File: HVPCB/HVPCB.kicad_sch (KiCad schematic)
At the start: 53 parts, among them J1 Micro Fit 10p, Q1 OnSemi FDB12N50TM, U1 NE555DR_C695838, U14 Micro Fit 2P, U16 Micro Fit 2P, U2 SN74LVC1GU04DBVR, U3 PDSE1-S5-D5-M-TR, U4 LM392MX, U5 AO3400A, U6 AO3400A, U7 KT-0603R, U8 KT-0603R, U9 KT-0603R

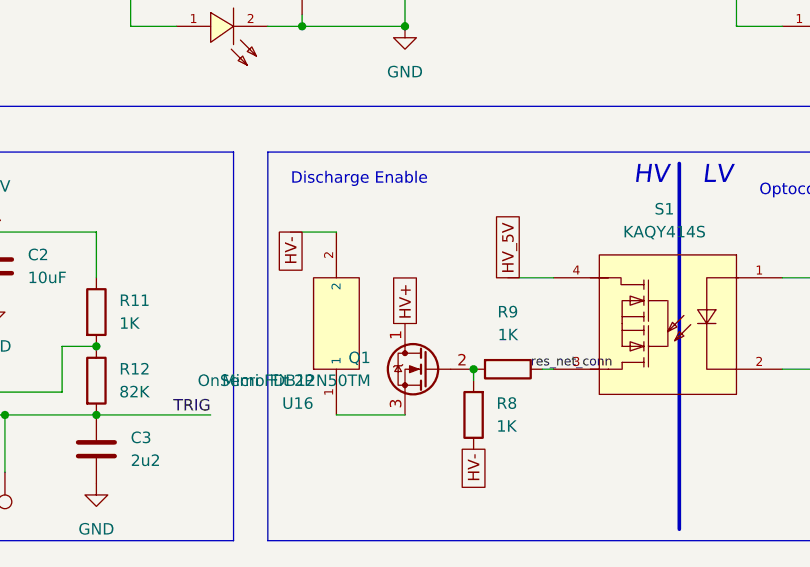
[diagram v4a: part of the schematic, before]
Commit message: switch to tht molex 1x10
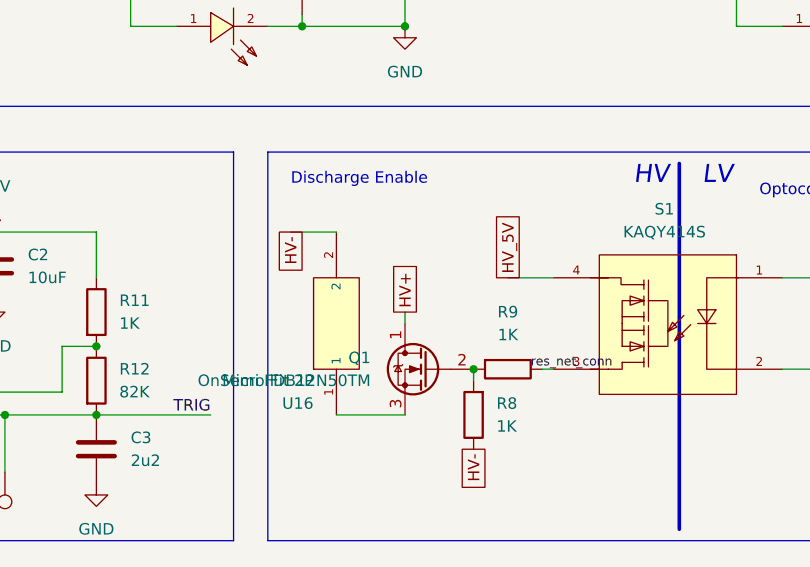
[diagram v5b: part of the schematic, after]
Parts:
- J1: footprint Connector_Molex:Molex_Micro-Fit_3.0_43650-1010_1x10-1MP_P3.00mm_Horizontal -> Connector_Molex:Molex_Micro-Fit_3.0_43650-1000_1x10_P3.00mm_Horizontal
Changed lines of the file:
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@@
+    (stroke (width 0) (type default) (color 0 0 0 0))
+  )
+  (wire (pts (xy 191.77 81.28) (xy 191.77 82.55))
     (stroke (width 0) (type default) (color 0 0 0 0))
   )
@@
     )
   )
-  (global_label "HV+" (shape passive) (at 191.77 82.55 90) (fields_autoplaced)
+  (global_label "HV+" (shape passive) (at 191.77 81.28 90) (fields_autoplaced)
     (effects (font (size 1.27 1.27)) (justify left))
-    (property "Intersheet References" "${INTERSHEET_REFS}" (id 0) (at 191.6906 76.1455 90)
+    (property "Intersheet References" "${INTERSHEET_REFS}" (id 0) (at 191.6906 74.8755 90)
       (effects (font (size 1.27 1.27)) (justify left) hide)
     )
@@
       (effects (font (size 1.27 1.27)) (justify left))
     )
-    (property "Footprint" "Connector_Molex:Molex_Micro-Fit_3.0_43650-1010_1x10-1MP_P3.00mm_Horizontal" (id 2) (at 81.28 35.56 0)
+    (property "Footprint" "Connector_Molex:Molex_Micro-Fit_3.0_43650-1000_1x10_P3.00mm_Horizontal" (id 2) (at 81.28 35.56 0)
       (effects (font (size 1.27 1.27)) hide)
     )
@@
     )
     (path "/44adef86-34ff-4db8-9923-04568cd6cc99"
-      (reference "J1") (unit 1) (value "Micro Fit 10p") (footprint "Connector_Molex:Molex_Micro-Fit_3.0_43650-1010_1x10-1MP_P3.00mm_Horizontal")
+      (reference "J1") (unit 1) (value "Micro Fit 10p") (footprint "Connector_Molex:Molex_Micro-Fit_3.0_43650-1000_1x10_P3.00mm_Horizontal")
     )
     (path "/36117206-a72e-44bf-83a9-33329a907e6a"

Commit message: HVPCB updates & assembly files
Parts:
- removed C1: 100nF, Resistor_SMD:R_0603_1608Metric_Pad0.98x0.95mm_HandSolder, symbol Device:C
- removed D2: 5V, footprint:LL-34_L3.5-W1.5-RD, symbol Device:D_Zener
- removed J1: Micro Fit 10p, Connector_Molex:Molex_Micro-Fit_3.0_43650-1000_1x10_P3.00mm_Horizontal, symbol Connector:Conn_01x10_Female
- removed Q1: OnSemi FDB12N50TM, Package_TO_SOT_SMD:TO-263-2_TabPin1_D2PAK, symbol Transistor_FET:BS170
- removed R2, R3: 10K, Resistor_SMD:R_0603_1608Metric_Pad0.98x0.95mm_HandSolder, symbol Device:R
- removed R8, R9: 1K, Resistor_SMD:R_0603_1608Metric_Pad0.98x0.95mm_HandSolder, symbol Device:R
- removed S1: KAQY414S, footprint:SOP-4_L3.9-W4.4-P2.54-LS7.0-BR, symbol default_lib:KAQY414S
- removed TP1: tp_Discharge, TestPoint:TestPoint_THTPad_D2.0mm_Drill1.0mm, symbol Connector:TestPoint
- removed U16: Micro Fit 2P, footprint:CONN-TH_43045-0200, symbol default_lib:0430450200
- added J1: MicroFit_8p, Connector_Molex:Molex_Micro-Fit_3.0_43650-0800_1x08_P3.00mm_Horizontal, symbol Connector:Conn_01x08_Female
- C2, C3, C4, C5: footprint Resistor_SMD:R_0603_1608Metric_Pad0.98x0.95mm_HandSolder -> Capacitor_SMD:C_0603_1608Metric_Pad1.08x0.95mm_HandSolder
- D1: value 5V -> 5v ZMM5V6-M; footprint footprint:LL-34_L3.5-W1.5-RD -> Diode_SMD:D_MiniMELF
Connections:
- net +5V: now also J1.2 (Pin_2)
- net GND: now also J1.1 (Pin_1), J1.3 (Pin_3), J1.6 (Pin_6), J1.8 (Pin_8)
- net G_TSAL: now also J1.5 (Pin_5)
- net HV_STATUS: now also J1.7 (Pin_7)
- net R_TSAL: now also J1.4 (Pin_4)
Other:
- note removed: "Discharge Enable"
